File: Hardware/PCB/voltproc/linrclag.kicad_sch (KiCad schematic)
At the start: 23 parts, among them J8 Jack, J9 Jack, U2 TL074, U3 TL072

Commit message: Redo layout
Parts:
- C10, C7, C8, C9: value 100nF -> (none); footprint ao_tht:C_Disc_D3.0mm_W1.6mm_P2.50mm -> (none)
- C3: value 47pF -> (none); footprint ao_tht:C_Disc_D3.0mm_W1.6mm_P2.50mm -> (none)
- C4: value 220nF -> (none); footprint ao_tht:C_Disc_D3.0mm_W1.6mm_P2.50mm -> (none)
- C5: value 2.2uF -> (none); footprint ao_tht:C_Radial_D8.0mm_H11.5mm_P3.50mm -> (none)
- C6: value 1uF -> (none); footprint ao_tht:C_Disc_D3.0mm_W1.6mm_P2.50mm -> (none)
- J8, J9: value Jack -> (none); footprint ao_tht:Jack_6.35mm_PJ_629HAN_slots -> (none)
- R1, R10: value 100k -> (none); footprint ao_tht:R_Axial_DIN0207_L6.3mm_D2.5mm_P10.16mm_Horizontal -> (none)
- R11: value 1k -> (none); footprint ao_tht:R_Axial_DIN0207_L6.3mm_D2.5mm_P10.16mm_Horizontal -> (none)
- R2, R3, R9: value 10k -> (none); footprint ao_tht:R_Axial_DIN0207_L6.3mm_D2.5mm_P10.16mm_Horizontal -> (none)
- R4: value 10M -> (none); footprint ao_tht:R_Axial_DIN0207_L6.3mm_D2.5mm_P10.16mm_Horizontal -> (none)
- R5: value 68k -> (none); footprint ao_tht:R_Axial_DIN0207_L6.3mm_D2.5mm_P10.16mm_Horizontal -> (none)
- R6: value 20k -> (none); footprint ao_tht:R_Axial_DIN0207_L6.3mm_D2.5mm_P10.16mm_Horizontal -> (none)
- R7: value 4.7k -> (none); footprint ao_tht:R_Axial_DIN0207_L6.3mm_D2.5mm_P10.16mm_Horizontal -> (none)
- R8: value 200R -> (none); footprint ao_tht:R_Axial_DIN0207_L6.3mm_D2.5mm_P10.16mm_Horizontal -> (none)
- U2: value TL074 -> (none); footprint ao_tht:DIP-14_W7.62mm_Socket_LongPads -> (none)
- U3: value TL072 -> (none); footprint ao_tht:DIP-8_W7.62mm_Socket_LongPads -> (none)

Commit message: Redo layout
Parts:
- removed C10, C9: (no value), symbol ao_symbols:C
- removed U3: (no value), symbol ao_symbols:TL072
- added C15, C16: 100nF, ao_tht:C_Disc_D3.0mm_W1.6mm_P2.50mm, symbol ao_symbols:C
- added U1: TL074, ao_tht:DIP-14_W7.62mm_Socket_LongPads, symbol Amplifier_Operational:TL074
- C3: value (none) -> 47pF; footprint (none) -> ao_tht:C_Disc_D5.0mm_W2.5mm_P5.00mm
- C4: value (none) -> 220nF; footprint (none) -> ao_tht:C_Rect_L7.2mm_W2.5mm_P5.00mm_FKS2_FKP2_MKS2_MKP2
- C5: value (none) -> 2.2uF; footprint (none) -> ao_tht:C_Radial_D8.0mm_H11.5mm_P3.50mm
- C6: value (none) -> 1uF; footprint (none) -> ao_tht:C_Rect_L7.2mm_W4.5mm_P5.00mm_FKS2_FKP2_MKS2_MKP2
- C7, C8: value (none) -> 100nF; footprint (none) -> ao_tht:C_Disc_D3.0mm_W1.6mm_P2.50mm
- J8, J9: value (none) -> Jack; footprint (none) -> ao_tht:Jack_6.35mm_PJ_629HAN_slots
- R1, R10: value (none) -> 100k; footprint (none) -> ao_tht:R_Axial_DIN0207_L6.3mm_D2.5mm_P10.16mm_Horizontal
- R11: value (none) -> 1k; footprint (none) -> ao_tht:R_Axial_DIN0207_L6.3mm_D2.5mm_P10.16mm_Horizontal
- R2, R3, R9: value (none) -> 10k; footprint (none) -> ao_tht:R_Axial_DIN0207_L6.3mm_D2.5mm_P10.16mm_Horizontal
- R4: value (none) -> 10M; footprint (none) -> ao_tht:R_Axial_DIN0207_L6.3mm_D2.5mm_P10.16mm_Horizontal
- R5: value (none) -> 68k; footprint (none) -> ao_tht:R_Axial_DIN0207_L6.3mm_D2.5mm_P10.16mm_Horizontal
- R6: value (none) -> 20k; footprint (none) -> ao_tht:R_Axial_DIN0207_L6.3mm_D2.5mm_P10.16mm_Horizontal
- R7: value (none) -> 4.7k; footprint (none) -> ao_tht:R_Axial_DIN0207_L6.3mm_D2.5mm_P10.16mm_Horizontal
- R8: value (none) -> 200R; footprint (none) -> ao_tht:R_Axial_DIN0207_L6.3mm_D2.5mm_P10.16mm_Horizontal
- U2: value (none) -> TL074; footprint (none) -> ao_tht:DIP-14_W7.62mm_Socket_LongPads
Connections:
- net +12V: now also C15.1, U1.4 (V+)
- net -12V: now also C16.2, U1.11 (V-)
- net GND: now also C15.2, C16.1, U1.5 (+)
- net LAG_RC_WIP: now also U1.3 (+)
- net RC_OUT: now also U1.1, U1.2 (-)
- new net: U1.6 (-), U1.7

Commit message: post breadboard revisions
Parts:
- C5: footprint ao_tht:C_Radial_D8.0mm_H11.5mm_P3.50mm -> ao_tht:C_Radial_D5.0mm_H11.0mm_P2.00mm
- C6: footprint ao_tht:C_Rect_L7.2mm_W4.5mm_P5.00mm_FKS2_FKP2_MKS2_MKP2 -> ao_tht:C_Rect_L7.2mm_W7.2mm_P5.00mm_FKS2_FKP2_MKS2_MKP2
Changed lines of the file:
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@@
     (comment 1 "or neighboring rights to this work. Published from United States.")
     (comment 2 "To the extent possible under law, Richard Holmes has waived all copyright and related ")
+    (comment 3 "Lag processor from MFOS design")
+    (comment 4 "From ARP 2600 schematics with updates and additions")
   )
   (junction (at 205.74 143.51) (diameter 0) (color 0 0 0 0)
@@
       (effects (font (size 1.27 1.27)) (justify left))
     )
-    (property "Footprint" "ao_tht:C_Radial_D8.0mm_H11.5mm_P3.50mm" (id 2) (at 126.6952 115.57 0)
+    (property "Footprint" "ao_tht:C_Radial_D5.0mm_H11.0mm_P2.00mm" (id 2) (at 126.6952 115.57 0)
       (effects (font (size 1.27 1.27)) hide)
     )
@@
     (property "Reference" "C6" (id 0) (at 200.66 55.1012 90))
     (property "Value" "1uF" (id 1) (at 200.66 57.6381 90))
-    (property "Footprint" "ao_tht:C_Rect_L7.2mm_W4.5mm_P5.00mm_FKS2_FKP2_MKS2_MKP2" (id 2) (at 204.47 59.9948 0)
-      (effects (font (size 1.27 1.27)) hide)
-    )
+    (property "Footprint" "ao_tht:C_Rect_L7.2mm_W7.2mm_P5.00mm_FKS2_FKP2_MKS2_MKP2" (id 2) (at 204.47 59.9948 0)
+      (effects (font (size 1.27 1.27)) hide)
+    )

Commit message: Pre fab tweaks, Gerbers, cap descriptions
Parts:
- renumbered C16 to C10, C15 to C9, U2 to U1, U1 to U2
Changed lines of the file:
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@@
+      (effects (font (size 1.27 1.27)) hide)
+    )
+    (property "Description" "Non polarized electrolytic capacitor" (id 5) (at 125.73 111.76 0)
       (effects (font (size 1.27 1.27)) hide)
     )
@@
   (symbol (lib_id "power:+12V") (at 223.52 135.89 0) (unit 1)
     (in_bom yes) (on_board yes)
-    (property "Reference" "#PWR038" (id 0) (at 223.52 139.7 0)
+    (property "Reference" "#PWR024" (id 0) (at 223.52 139.7 0)
       (effects (font (size 1.27 1.27)) hide)
     )
@@
   (symbol (lib_id "Amplifier_Operational:TL074") (at 191.77 143.51 0) (unit 5)
     (in_bom yes) (on_board yes) (fields_autoplaced)
-    (property "Reference" "U2" (id 0) (at 189.865 142.6753 0)
+    (property "Reference" "U1" (id 0) (at 189.865 142.6753 0)
       (effects (font (size 1.27 1.27)) (justify left))
     )
@@
   (symbol (lib_id "power:-12V") (at 205.74 151.13 180) (unit 1)
     (in_bom yes) (on_board yes)
-    (property "Reference" "#PWR012" (id 0) (at 205.74 153.67 0)
+    (property "Reference" "#PWR022" (id 0) (at 205.74 153.67 0)
       (effects (font (size 1.27 1.27)) hide)
     )
@@
       (effects (font (size 1.27 1.27)) hide)
     )
+    (property "Description" "Ceramic capacitor" (id 5) (at 106.68 69.85 0)
+      (effects (font (size 1.27 1.27)) hide)
+    )
     (pin "1")
     (pin "2")
@@
   (symbol (lib_id "power:GND") (at 234.95 114.3 0) (unit 1)
     (in_bom yes) (on_board yes) (fields_autoplaced)
-    (property "Reference" "#PWR015" (id 0) (at 234.95 120.65 0)
+    (property "Reference" "#PWR027" (id 0) (at 234.95 120.65 0)
       (effects (font (size 1.27 1.27)) hide)
     )
@@
   (symbol (lib_id "ao_symbols:C") (at 223.52 139.7 0) (unit 1)
     (in_bom yes) (on_board yes)
-    (property "Reference" "C15" (id 0) (at 226.441 138.5316 0)
+    (property "Reference" "C9" (id 0) (at 226.441 138.5316 0)
       (effects (font (size 1.27 1.27)) (justify left))
     )
@@
     )
     (property "SKU" "A-553" (id 5) (at 223.52 139.7 0)
+      (effects (font (size 1.27 1.27)) hide)
+    )
+    (property "Description" "Ceramic capacitor" (id 6) (at 223.52 139.7 0)
       (effects (font (size 1.27 1.27)) hide)
     )
@@
       (effects (font (size 1.27 1.27)) hide)
     )
+    (property "Description" "Film capacitor" (id 5) (at 200.66 60.96 0)
+      (effects (font (size 1.27 1.27)) hide)
+    )
     (pin "1")
     (pin "2")
@@
   (symbol (lib_id "Amplifier_Operational:TL074") (at 237.49 143.51 0) (unit 5)
     (in_bom yes) (on_board yes) (fields_autoplaced)
-    (property "Reference" "U1" (id 0) (at 235.585 142.6753 0)
+    (property "Reference" "U2" (id 0) (at 235.585 142.6753 0)
       (effects (font (size 1.27 1.27)) (justify left))
     )
@@
   (symbol (lib_id "power:GND") (at 217.17 143.51 0) (unit 1)
     (in_bom yes) (on_board yes)
-    (property "Reference" "#PWR033" (id 0) (at 217.17 149.86 0)
+    (property "Reference" "#PWR023" (id 0) (at 217.17 149.86 0)
       (effects (font (size 1.27 1.27)) hide)
     )
@@
   (symbol (lib_id "power:GND") (at 35.56 57.15 0) (unit 1)
     (in_bom yes) (on_board yes) (fields_autoplaced)
-    (property "Reference" "#PWR05" (id 0) (at 35.56 63.5 0)
+    (property "Reference" "#PWR015" (id 0) (at 35.56 63.5 0)
       (effects (font (size 1.27 1.27)) hide)
     )
@@
   (symbol (lib_id "power:GND") (at 130.81 72.39 0) (unit 1)
     (in_bom yes) (on_board yes) (fields_autoplaced)
-    (property "Reference" "#PWR08" (id 0) (at 130.81 78.74 0)
+    (property "Reference" "#PWR018" (id 0) (at 130.81 78.74 0)
       (effects (font (size 1.27 1.27)) hide)
     )
@@
   (symbol (lib_id "power:GND") (at 254 57.15 0) (mirror y) (unit 1)
     (in_bom yes) (on_board yes) (fields_autoplaced)
-    (property "Reference" "#PWR018" (id 0) (at 254 63.5 0)
+    (property "Reference" "#PWR028" (id 0) (at 254 63.5 0)
       (effects (font (size 1.27 1.27)) hide)
     )
@@
   (symbol (lib_id "power:GND") (at 233.68 63.5 0) (unit 1)
     (in_bom yes) (on_board yes) (fields_autoplaced)
-    (property "Reference" "#PWR014" (id 0) (at 233.68 69.85 0)
+    (property "Reference" "#PWR026" (id 0) (at 233.68 69.85 0)
       (effects (font (size 1.27 1.27)) hide)
     )
@@
   (symbol (lib_id "power:GND") (at 199.39 143.51 0) (unit 1)
     (in_bom yes) (on_board yes)
-    (property "Reference" "#PWR010" (id 0) (at 199.39 149.86 0)
+    (property "Reference" "#PWR020" (id 0) (at 199.39 149.86 0)
       (effects (font (size 1.27 1.27)) hide)
     )
@@
       (effects (font (size 1.27 1.27)) hide)
     )
+    (property "Description" "Ceramic capacitor" (id 6) (at 205.74 147.32 0)
+      (effects (font (size 1.27 1.27)) hide)
+    )
     (pin "1")
     (pin "2")
@@
   (symbol (lib_id "Amplifier_Operational:TL074") (at 142.24 53.34 0) (unit 3)
     (in_bom yes) (on_board yes) (fields_autoplaced)
-    (property "Reference" "U2" (id 0) (at 142.24 44.5602 0))
+    (property "Reference" "U1" (id 0) (at 142.24 44.5602 0))
     (property "Value" "TL074" (id 1) (at 142.24 47.0971 0))
     (property "Footprint" "ao_tht:DIP-14_W7.62mm_Socket_LongPads" (id 2) (at 140.97 50.8 0)
@@
       (effects (font (size 1.27 1.27)) hide)
     )
+    (property "Description" "Film capacitor" (id 5) (at 113.03 111.76 0)
+      (effects (font (size 1.27 1.27)) hide)
+    )
     (pin "1")
     (pin "2")
@@
   (symbol (lib_id "Amplifier_Operational:TL074") (at 199.39 50.8 0) (unit 4)
     (in_bom yes) (on_board yes) (fields_autoplaced)
-    (property "Reference" "U2" (id 0) (at 199.39 42.0202 0))
+    (property "Reference" "U1" (id 0) (at 199.39 42.0202 0))
     (property "Value" "TL074" (id 1) (at 199.39 44.5571 0))
     (property "Footprint" "ao_tht:DIP-14_W7.62mm_Socket_LongPads" (id 2) (at 198.12 48.26 0)
@@
   (symbol (lib_id "Amplifier_Operational:TL074") (at 110.49 50.8 0) (unit 2)
     (in_bom yes) (on_board yes) (fields_autoplaced)
-    (property "Reference" "U2" (id 0) (at 110.49 42.0202 0))
+    (property "Reference" "U1" (id 0) (at 110.49 42.0202 0))
     (property "Value" "TL074" (id 1) (at 110.49 44.5571 0))
     (property "Footprint" "ao_tht:DIP-14_W7.62mm_Socket_LongPads" (id 2) (at 109.22 48.26 0)
@@
       (effects (font (size 1.27 1.27)) hide)
     )
+    (property "Description" "Ceramic capacitor" (id 6) (at 205.74 139.7 0)
+      (effects (font (size 1.27 1.27)) hide)
+    )
     (pin "1")
     (pin "2")
@@
   (symbol (lib_id "power:+12V") (at 205.74 135.89 0) (unit 1)
     (in_bom yes) (on_board yes)
-    (property "Reference" "#PWR011" (id 0) (at 205.74 139.7 0)
+    (property "Reference" "#PWR021" (id 0) (at 205.74 139.7 0)
       (effects (font (size 1.27 1.27)) hide)
     )
@@
   (symbol (lib_id "power:GND") (at 41.91 66.04 0) (unit 1)
     (in_bom yes) (on_board yes) (fields_autoplaced)
-    (property "Reference" "#PWR06" (id 0) (at 41.91 72.39 0)
+    (property "Reference" "#PWR016" (id 0) (at 41.91 72.39 0)
       (effects (font (size 1.27 1.27)) hide)
     )
@@
   (symbol (lib_id "ao_symbols:C") (at 223.52 147.32 0) (unit 1)
     (in_bom yes) (on_board yes)
-    (property "Reference" "C16" (id 0) (at 226.441 146.1516 0)
+    (property "Reference" "C10" (id 0) (at 226.441 146.1516 0)
       (effects (font (size 1.27 1.27)) (justify left))
     )
@@
     )
     (property "SKU" "A-553" (id 5) (at 223.52 147.32 0)
+      (effects (font (size 1.27 1.27)) hide)
+    )
+    (property "Description" "Ceramic capacitor" (id 6) (at 223.52 147.32 0)
       (effects (font (size 1.27 1.27)) hide)
     )
@@
   (symbol (lib_id "Amplifier_Operational:TL074") (at 243.84 110.49 0) (mirror x) (unit 2)
     (in_bom yes) (on_board yes)
-    (property "Reference" "U1" (id 0) (at 243.84 102.87 0))
+    (property "Reference" "U2" (id 0) (at 243.84 102.87 0))
     (property "Value" "TL074" (id 1) (at 243.84 105.41 0))
     (property "Footprint" "ao_tht:DIP-14_W7.62mm_Socket_LongPads" (id 2) (at 242.57 113.03 0)
@@
   (symbol (lib_id "power:GND") (at 113.03 116.84 0) (unit 1)
     (in_bom yes) (on_board yes) (fields_autoplaced)
-    (property "Reference" "#PWR07" (id 0) (at 113.03 123.19 0)
+    (property "Reference" "#PWR017" (id 0) (at 113.03 123.19 0)
       (effects (font (size 1.27 1.27)) hide)
     )
@@
   (symbol (lib_id "power:GND") (at 187.96 41.91 0) (unit 1)
     (in_bom yes) (on_board yes) (fields_autoplaced)
-    (property "Reference" "#PWR09" (id 0) (at 187.96 48.26 0)
+    (property "Reference" "#PWR019" (id 0) (at 187.96 48.26 0)
       (effects (font (size 1.27 1.27)) hide)
     )
@@
   (symbol (lib_id "power:-12V") (at 223.52 151.13 180) (unit 1)
     (in_bom yes) (on_board yes)
-    (property "Reference" "#PWR039" (id 0) (at 223.52 153.67 0)
+    (property "Reference" "#PWR025" (id 0) (at 223.52 153.67 0)
       (effects (font (size 1.27 1.27)) hide)
     )
@@
   (symbol (lib_id "Amplifier_Operational:TL074") (at 148.59 104.14 0) (mirror x) (unit 1)
     (in_bom yes) (on_board yes)
-    (property "Reference" "U1" (id 0) (at 148.59 96.52 0))
+    (property "Reference" "U2" (id 0) (at 148.59 96.52 0))
     (property "Value" "TL074" (id 1) (at 148.59 99.06 0))
     (property "Footprint" "ao_tht:DIP-14_W7.62mm_Socket_LongPads" (id 2) (at 147.32 106.68 0)
@@
   (symbol (lib_id "Amplifier_Operational:TL074") (at 59.69 55.88 0) (unit 1)
     (in_bom yes) (on_board yes) (fields_autoplaced)
-    (property "Reference" "U2" (id 0) (at 59.69 47.1002 0))
+    (property "Reference" "U1" (id 0) (at 59.69 47.1002 0))
     (property "Value" "TL074" (id 1) (at 59.69 49.6371 0))
     (property "Footprint" "ao_tht:DIP-14_W7.62mm_Socket_LongPads" (id 2) (at 58.42 53.34 0)

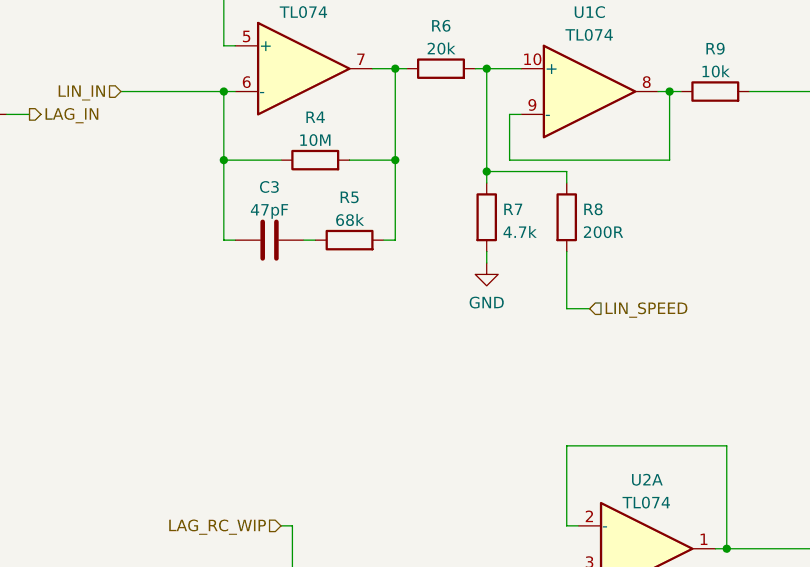
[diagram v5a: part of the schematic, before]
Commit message: R7->47k; documentation and photos
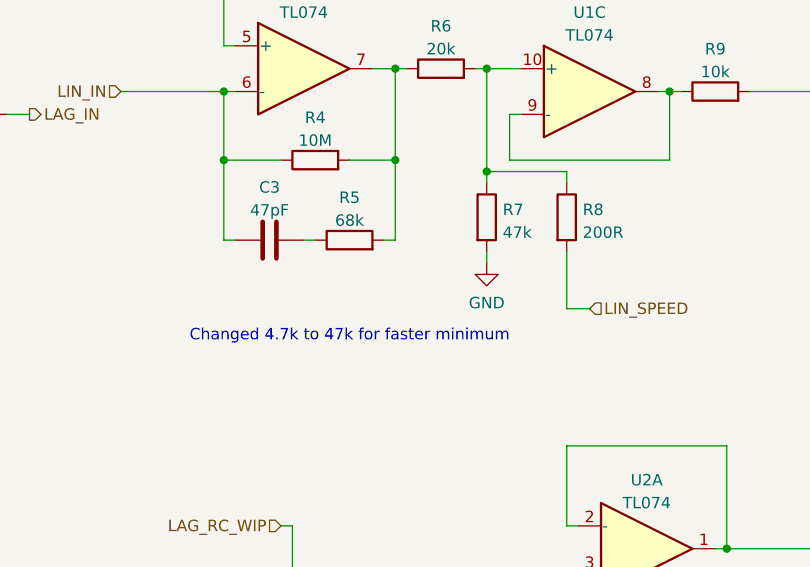
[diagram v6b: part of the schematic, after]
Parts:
- C4: SKU (none) -> A-984
- C5: SKU (none) -> A-4223
- C6: SKU (none) -> A-4755
- R7: value 4.7k -> 47k
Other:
- note added: "Changed 4.7k to 47k for faster minimum"
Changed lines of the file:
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@@
     (effects (font (size 1.27 1.27)) (justify right bottom))
+  )
+  (text "Changed 4.7k to 47k for faster minimum" (at 97.79 81.28 0)
+    (effects (font (size 1.27 1.27)) (justify left bottom))
   )
   (label "OUT_LAG_B" (at 254 53.34 180)
@@
       (effects (font (size 1.27 1.27)) hide)
     )
-    (property "Description" "Non polarized electrolytic capacitor" (id 5) (at 125.73 111.76 0)
+    (property "Description" "Non polarized electrolytic capacitor, 2.5 mm pitch" (id 5) (at 125.73 111.76 0)
+      (effects (font (size 1.27 1.27)) hide)
+    )
+    (property "SKU" "A-4223" (id 6) (at 125.73 111.76 0)
       (effects (font (size 1.27 1.27)) hide)
     )
@@
     )
     (property "Datasheet" "http://www.ti.com/lit/ds/symlink/tl071.pdf" (id 3) (at 193.04 138.43 0)
+      (effects (font (size 1.27 1.27)) hide)
+    )
+    (property "Description" "Quad op amp, DIP-14" (id 4) (at 191.77 143.51 0)
       (effects (font (size 1.27 1.27)) hide)
     )
@@
       (effects (font (size 1.27 1.27)) hide)
     )
-    (property "Description" "Ceramic capacitor" (id 5) (at 106.68 69.85 0)
+    (property "Description" "Ceramic capacitor, 5 mm pitch" (id 5) (at 106.68 69.85 0)
       (effects (font (size 1.27 1.27)) hide)
     )
@@
       (effects (font (size 1.27 1.27)) hide)
     )
-    (property "Description" "Ceramic capacitor" (id 6) (at 223.52 139.7 0)
+    (property "Description" "Ceramic capacitor, 2.5 mm pitch" (id 6) (at 223.52 139.7 0)
       (effects (font (size 1.27 1.27)) hide)
     )
@@
       (effects (font (size 1.27 1.27)) hide)
     )
-    (property "Description" "Film capacitor" (id 5) (at 200.66 60.96 0)
+    (property "Description" "Film capacitor, 5 mm pitch" (id 5) (at 200.66 60.96 0)
+      (effects (font (size 1.27 1.27)) hide)
+    )
+    (property "SKU" "A-4755" (id 6) (at 200.66 60.96 0)
       (effects (font (size 1.27 1.27)) hide)
     )
@@
     )
     (property "Datasheet" "http://www.ti.com/lit/ds/symlink/tl071.pdf" (id 3) (at 238.76 138.43 0)
+      (effects (font (size 1.27 1.27)) hide)
+    )
+    (property "Description" "Quad op amp, DIP-14" (id 4) (at 237.49 143.51 0)
       (effects (font (size 1.27 1.27)) hide)
     )
@@
       (effects (font (size 1.27 1.27)) hide)
     )
-    (property "Description" "Ceramic capacitor" (id 6) (at 205.74 147.32 0)
+    (property "Description" "Ceramic capacitor, 2.5 mm pitch" (id 6) (at 205.74 147.32 0)
       (effects (font (size 1.27 1.27)) hide)
     )
@@
     )
     (property "Datasheet" "http://www.ti.com/lit/ds/symlink/tl071.pdf" (id 3) (at 143.51 48.26 0)
+      (effects (font (size 1.27 1.27)) hide)
+    )
+    (property "Description" "Quad op amp, DIP-14" (id 4) (at 142.24 53.34 0)
       (effects (font (size 1.27 1.27)) hide)
     )
@@
       (effects (font (size 1.27 1.27)) hide)
     )
+    (property "Description" "1/4\" audio jack" (id 4) (at 260.35 53.34 0)
+      (effects (font (size 1.27 1.27)) hide)
+    )
     (pin "S")
     (pin "T")
@@
       (effects (font (size 1.27 1.27)) hide)
     )
-    (property "Description" "Film capacitor" (id 5) (at 113.03 111.76 0)
+    (property "Description" "Film capacitor, 5 mm pitch" (id 5) (at 113.03 111.76 0)
+      (effects (font (size 1.27 1.27)) hide)
+    )
+    (property "SKU" "A-984" (id 6) (at 113.03 111.76 0)
       (effects (font (size 1.27 1.27)) hide)
     )
@@
     )
     (property "Datasheet" "http://www.ti.com/lit/ds/symlink/tl071.pdf" (id 3) (at 200.66 45.72 0)
+      (effects (font (size 1.27 1.27)) hide)
+    )
+    (property "Description" "Quad op amp, DIP-14" (id 4) (at 199.39 50.8 0)
       (effects (font (size 1.27 1.27)) hide)
     )
@@
       (effects (font (size 1.27 1.27)) hide)
     )
+    (property "Description" "Quad op amp, DIP-14" (id 4) (at 110.49 50.8 0)
+      (effects (font (size 1.27 1.27)) hide)
+    )
     (pin "1")
     (pin "2")
@@
       (effects (font (size 1.27 1.27)) hide)
     )
-    (property "Description" "Ceramic capacitor" (id 6) (at 205.74 139.7 0)
+    (property "Description" "Ceramic capacitor, 2.5 mm pitch" (id 6) (at 205.74 139.7 0)
       (effects (font (size 1.27 1.27)) hide)
     )
@@
       (effects (font (size 1.27 1.27)) (justify left))
     )
-    (property "Value" "4.7k" (id 1) (at 132.588 69.0122 0)
+    (property "Value" "47k" (id 1) (at 132.588 69.0122 0)
       (effects (font (size 1.27 1.27)) (justify left))
     )
@@
       (effects (font (size 1.27 1.27)) hide)
     )
-    (property "Description" "Ceramic capacitor" (id 6) (at 223.52 147.32 0)
+    (property "Description" "Ceramic capacitor, 2.5 mm pitch" (id 6) (at 223.52 147.32 0)
       (effects (font (size 1.27 1.27)) hide)
     )
@@
     )
     (property "Datasheet" "http://www.ti.com/lit/ds/symlink/tl071.pdf" (id 3) (at 245.11 115.57 0)
+      (effects (font (size 1.27 1.27)) hide)
+    )
+    (property "Description" "Quad op amp, DIP-14" (id 4) (at 243.84 110.49 0)
       (effects (font (size 1.27 1.27)) hide)
     )
@@
       (effects (font (size 1.27 1.27)) hide)
     )
+    (property "Description" "Quad op amp, DIP-14" (id 4) (at 148.59 104.14 0)
+      (effects (font (size 1.27 1.27)) hide)
+    )
     (pin "1")
     (pin "2")
@@
       (effects (font (size 1.27 1.27)) hide)
     )
+    (property "Description" "Quad op amp, DIP-14" (id 4) (at 59.69 55.88 0)
+      (effects (font (size 1.27 1.27)) hide)
+    )
     (pin "1")
     (pin "2")
@@
       (effects (font (size 1.27 1.27)) hide)
     )
+    (property "Description" "1/4\" audio jack" (id 4) (at 29.21 53.34 0)
+      (effects (font (size 1.27 1.27)) hide)
+    )
